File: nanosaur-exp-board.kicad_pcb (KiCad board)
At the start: 2 copper layers, 80 x 20 mm, 13 parts, among them J1 jetson_nano, J2 Screw_Terminal_01x02, J3 Conn_oled_right, J4 Conn_oled_left, J5 Conn_motors, J6 Conn_01x03, SW1 SW_SPDT

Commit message: minor fixes
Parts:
- J1: footprint Connector_PinSocket_2.54mm:PinSocket_2x21_P2.54mm_Vertical -> Connector_PinSocket_2.54mm:PinSocket_2x20_P2.54mm_Vertical
- moved J2 2.84 mm to (157.3, 92.8)
- moved J3 2.84 mm to (135.5, 86.0)
- moved J4 2.84 mm to (145.7, 86.0)
- moved J5 2.84 mm to (145.7, 89.8)
- moved J6 2.84 mm to (132.9, 89.8)
- moved R1 2.84 mm to (138.1, 92.8)
- moved R2 2.84 mm to (138.1, 95.1)
- moved J1 2.72 mm to (163.6, 97.9)
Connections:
- J1 pad 10: Net-(J1-Pad10) -> (no net)
- J1 pad 11: Net-(J1-Pad11) -> (no net)
- J1 pad 12: Net-(J1-Pad12) -> (no net)
- J1 pad 13: Net-(J1-Pad13) -> (no net)
- J1 pad 15: Net-(J1-Pad15) -> (no net)
- J1 pad 16: Net-(J1-Pad16) -> (no net)
- J1 pad 18: Net-(J1-Pad18) -> (no net)
- J1 pad 19: Net-(J1-Pad19) -> (no net)
- J1 pad 21: Net-(J1-Pad21) -> (no net)
- J1 pad 22: Net-(J1-Pad22) -> (no net)
- J1 pad 23: Net-(J1-Pad23) -> (no net)
- J1 pad 24: Net-(J1-Pad24) -> (no net)
- J1 pad 26: Net-(J1-Pad26) -> (no net)
- J1 pad 29: Net-(J1-Pad29) -> (no net)
- J1 pad 32: Net-(J1-Pad32) -> (no net)
- J1 pad 35: Net-(J1-Pad35) -> (no net)
- J1 pad 36: Net-(J1-Pad36) -> (no net)
- J1 pad 37: Net-(J1-Pad37) -> (no net)
- J1 pad 38: Net-(J1-Pad38) -> (no net)
- J1 pad 40: Net-(J1-Pad40) -> (no net)
- J1 pad 7: Net-(J1-Pad7) -> (no net)
- J1 pad 8: Net-(J1-Pad8) -> (no net)
- SW1 pad 3: Net-(SW1-Pad3) -> (no net)
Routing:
- net VCC: track 76.9 -> 64.9 mm
- net Net-(J2-Pad2): track 15.0 -> 16.7 mm

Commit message: Merge update from Mauro and minor fixes
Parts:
- J1: footprint Connector_PinSocket_2.54mm:PinSocket_2x20_P2.54mm_Vertical -> Connector_PinSocket_2.54mm:PinSocket_2x21_P2.54mm_Vertical
- moved J2 2.84 mm to (160.0, 91.9)
- moved J4 2.84 mm to (148.4, 85.2)
- moved J5 2.84 mm to (148.4, 89.0)
- moved J6 2.84 mm to (135.6, 88.9)
- moved R1 2.84 mm to (140.8, 91.9)
- moved R2 2.84 mm to (140.8, 94.2)
- moved J1 2.72 mm to (166.2, 97.0)
- moved J3 1.87 mm to (137.2, 85.2)
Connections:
- J1 pad 10: (no net) -> Net-(J1-Pad10)
- J1 pad 11: (no net) -> Net-(J1-Pad11)
- J1 pad 12: (no net) -> Net-(J1-Pad12)
- J1 pad 13: (no net) -> Net-(J1-Pad13)
- J1 pad 15: (no net) -> Net-(J1-Pad15)
- J1 pad 16: (no net) -> Net-(J1-Pad16)
- J1 pad 18: (no net) -> Net-(J1-Pad18)
- J1 pad 19: (no net) -> Net-(J1-Pad19)
- J1 pad 21: (no net) -> Net-(J1-Pad21)
- J1 pad 22: (no net) -> Net-(J1-Pad22)
- J1 pad 23: (no net) -> Net-(J1-Pad23)
- J1 pad 24: (no net) -> Net-(J1-Pad24)
- J1 pad 26: (no net) -> Net-(J1-Pad26)
- J1 pad 29: (no net) -> Net-(J1-Pad29)
- J1 pad 32: (no net) -> Net-(J1-Pad32)
- J1 pad 35: (no net) -> Net-(J1-Pad35)
- J1 pad 36: (no net) -> Net-(J1-Pad36)
- J1 pad 37: (no net) -> Net-(J1-Pad37)
- J1 pad 38: (no net) -> Net-(J1-Pad38)
- J1 pad 40: (no net) -> Net-(J1-Pad40)
- J1 pad 7: (no net) -> Net-(J1-Pad7)
- J1 pad 8: (no net) -> Net-(J1-Pad8)
- SW1 pad 3: (no net) -> Net-(SW1-Pad3)
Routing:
- net GND: track 3.81 -> 131.6 mm, vias 0 -> 1
- net +3V3: track 9.93 -> 37.8 mm, vias 0 -> 2
- net VCC: track 64.9 -> 77.6 mm
- net Net-(J2-Pad2): track 16.7 -> 15.0 mm
- net Net-(J1-Pad28): track 18.8 -> 19.4 mm, vias 0 -> 1
- added copper zone on B.Cu, net GND
- added copper zone on F.Cu, net GND
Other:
- net class POWER added: clearance 0.2, trace_width 0.35, via_dia 0.8, via_drill 0.4

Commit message: Improve sch and pcb
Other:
- board text added: "Nanosaur expansion board"
- board text added: "Raffaello Bonghi"
- board text added: "v1.0"

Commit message: Improve pcb
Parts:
- moved SW1 0.88 mm to (171.6, 94.2)
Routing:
- net VCC: track 77.6 -> 76.2 mm

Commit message: Improve sch and pcb
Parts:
- added G***: LOGO, nanosaur:nanosaur_logo, F.Cu at (121.2, 91.8)
- added H5: MountingHole, MountingHole:MountingHole_2.2mm_M2, F.Cu at (116.0, 85.8)
- added H6: MountingHole, MountingHole:MountingHole_2.2mm_M2, F.Cu at (122.0, 85.8)
- added J7: Conn_01x04, Connector_PinHeader_2.54mm:PinHeader_1x04_P2.54mm_Vertical, F.Cu at (147.5, 93.2)
- H1, H2, H3, H4: footprint MountingHole:MountingHole_2.2mm_M2_ISO7380_Pad -> MountingHole:MountingHole_2.2mm_M2
- J3: value Conn_oled_right -> Conn_01x04
- J4: value Conn_oled_left -> Conn_01x04
- J5: value Conn_motors -> Conn_01x06; footprint Connector_PinHeader_2.54mm:PinHeader_1x04_P2.54mm_Vertical -> Connector_PinHeader_2.54mm:PinHeader_1x06_P2.54mm_Vertical
- moved J5 4.25 mm to (152.6, 89.5)
- moved R2 3.81 mm to (137.1, 94.6)
- moved R1 3.80 mm to (137.1, 92.4)
- moved J2 2.59 mm to (160.1, 94.5)
- moved J6 2.08 mm to (133.6, 89.5)
- moved J1 1.41 mm to (166.6, 98.4)
- moved J3 1.16 mm to (136.2, 85.8)
- moved J4 1.10 mm to (147.5, 85.8)
- moved SW1 0.20 mm to (171.6, 94.4)
- moved H1 0.06 mm to (109.0, 85.3)
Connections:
- J1 pad 10: Net-(J1-Pad10) -> (no net)
- J1 pad 11: Net-(J1-Pad11) -> (no net)
- J1 pad 12: Net-(J1-Pad12) -> (no net)
- J1 pad 13: Net-(J1-Pad13) -> (no net)
- J1 pad 15: Net-(J1-Pad15) -> (no net)
- J1 pad 16: Net-(J1-Pad16) -> (no net)
- J1 pad 18: Net-(J1-Pad18) -> (no net)
- J1 pad 19: Net-(J1-Pad19) -> (no net)
- J1 pad 21: Net-(J1-Pad21) -> (no net)
- J1 pad 22: Net-(J1-Pad22) -> (no net)
- J1 pad 23: Net-(J1-Pad23) -> (no net)
- J1 pad 24: Net-(J1-Pad24) -> (no net)
- J1 pad 26: Net-(J1-Pad26) -> (no net)
- J1 pad 29: Net-(J1-Pad29) -> (no net)
- J1 pad 32: Net-(J1-Pad32) -> (no net)
- J1 pad 35: Net-(J1-Pad35) -> (no net)
- J1 pad 36: Net-(J1-Pad36) -> (no net)
- J1 pad 37: Net-(J1-Pad37) -> (no net)
- J1 pad 38: Net-(J1-Pad38) -> (no net)
- J1 pad 40: Net-(J1-Pad40) -> (no net)
- J1 pad 7: Net-(J1-Pad7) -> (no net)
- J1 pad 8: Net-(J1-Pad8) -> (no net)
- J3 pad 3: VCC -> +3V3
- J4 pad 3: VCC -> +3V3
- J5 pad 1: Net-(J1-Pad3) -> VCC
- J5 pad 2: Net-(J1-Pad5) -> GND
- J5 pad 3: VCC -> Net-(J1-Pad3)
- J5 pad 4: GND -> Net-(J1-Pad5)
- SW1 pad 3: Net-(SW1-Pad3) -> (no net)
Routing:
- net GND: track 131.6 -> 88.2 mm, vias 1 -> 0
- net VCC: track 76.2 -> 48.3 mm
- net +3V3: track 37.8 -> 63.1 mm, vias 2 -> 0
- net Net-(J2-Pad2): track 15.0 -> 17.7 mm
- net Net-(J1-Pad31): track 15.0 -> 12.3 mm
- net Net-(J1-Pad33): track 15.3 -> 12.7 mm
- net Net-(J1-Pad27): track 16.5 -> 14.5 mm
- net Net-(J1-Pad5): track 25.5 -> 27.2 mm
- net Net-(J1-Pad3): track 26.2 -> 27.7 mm
- net Net-(J1-Pad28): track 19.4 -> 19.6 mm, vias 1 -> 0
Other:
- outline, holes or cut-outs redrawn
- net class 3.3 line added: clearance 0.2, trace_width 0.45, via_dia 0.8, via_drill 0.4
- net class POWER: trace_width 0.35 -> 1.3

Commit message: Improve sch and azz gerber zip
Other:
- board text added: "(C)2021 Raffaello Bonghi"
- board text added: "nanosaur.ai"
- board text removed: "Raffaello Bonghi"

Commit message: Fix kibot and pcb
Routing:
- net GND: track 88.2 -> 84.2 mm
- net Net-(J2-Pad2): track 17.7 -> 14.8 mm
- net VCC: track 48.3 -> 46.2 mm

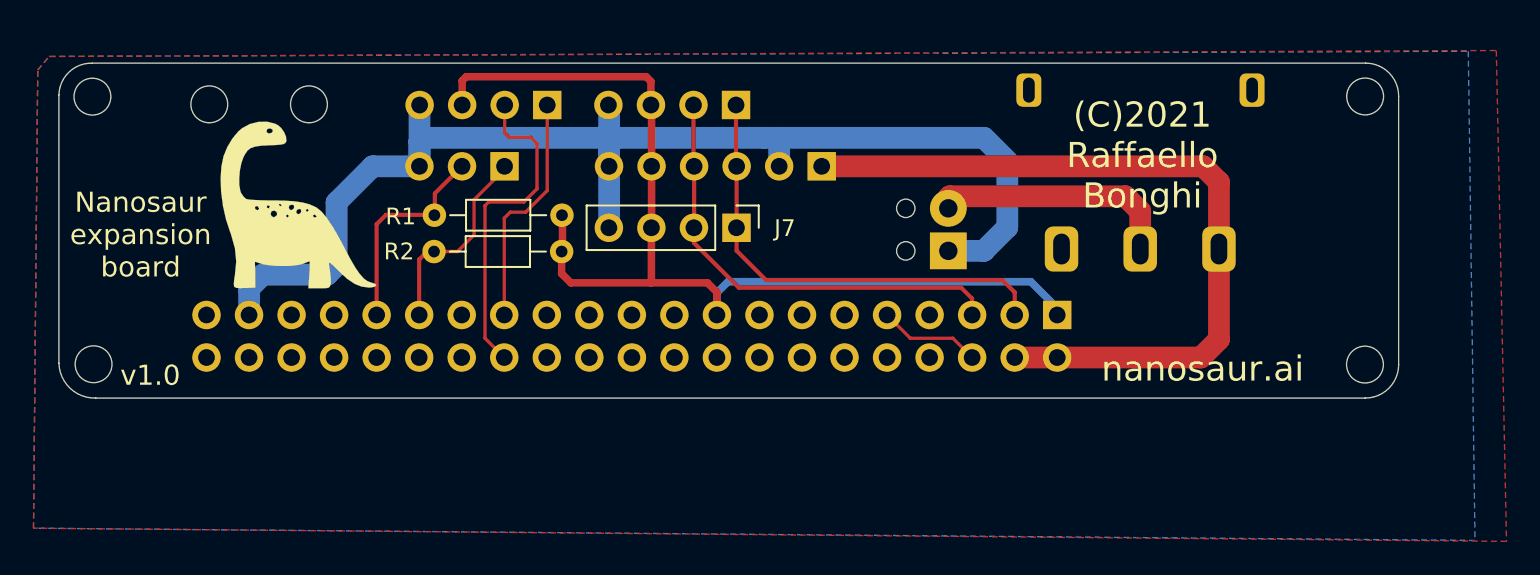
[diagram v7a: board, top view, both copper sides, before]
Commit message: Improve PCB layout, fix BOM, improve sch
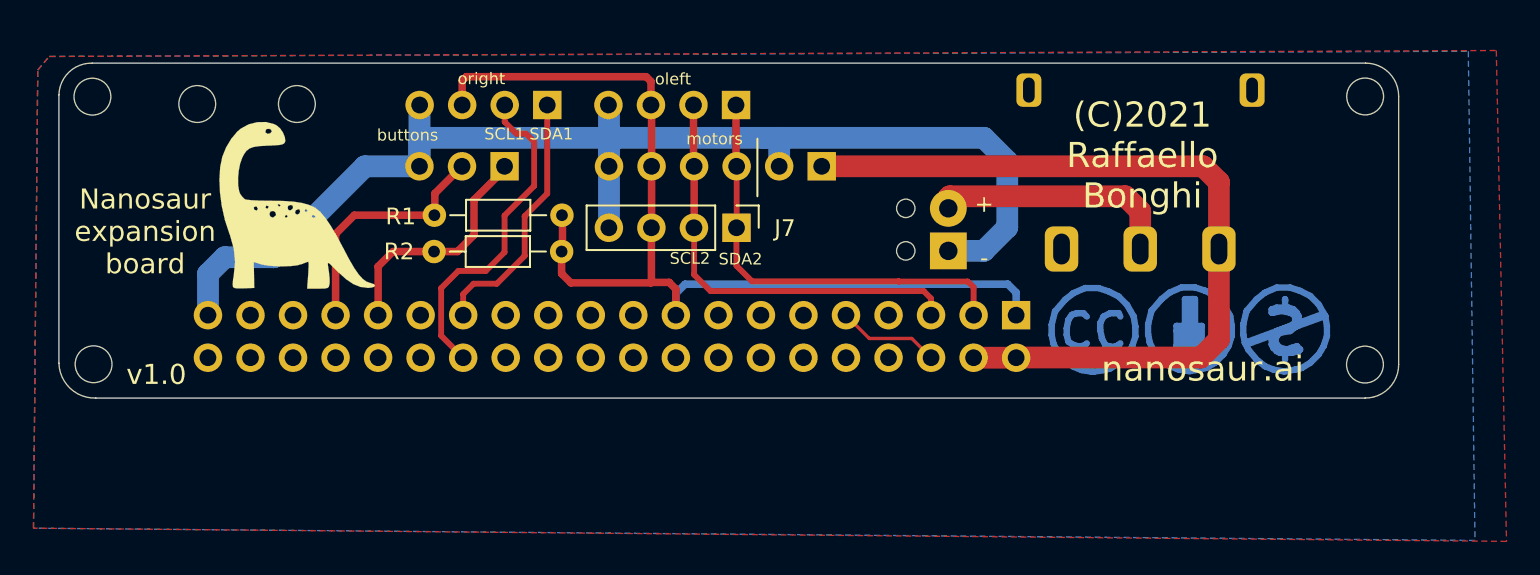
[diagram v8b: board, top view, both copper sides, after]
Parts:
- added G***: LOGO, nanosaur:officinerobotiche, B.Cu at (111.3, 91.8)
- added REF**: Symbol_CreativeCommons_CopperTop_Type2_Small, Symbol:Symbol_CreativeCommons_CopperTop_Type2_Small, B.Cu at (168.7, 99.2)
- added REF**: Symbol_CC-Noncommercial_CopperTop_Small, Symbol:Symbol_CC-Noncommercial_CopperTop_Small, B.Cu at (180.2, 99.2)
- added REF**: Symbol_CC-Attribution_CopperTop_Small, Symbol:Symbol_CC-Attribution_CopperTop_Small, B.Cu at (174.6, 99.2)
- J1: footprint Connector_PinSocket_2.54mm:PinSocket_2x21_P2.54mm_Vertical -> Connector_PinSocket_2.54mm:PinSocket_2x20_P2.54mm_Vertical
- J3, J4: value Conn_01x04 -> Conn_i2c_oled
- J5: value Conn_01x06 -> Conn_motors
- J6: value Conn_01x03 -> Conn_buttons
- moved J1 2.45 mm to (164.2, 98.4)
- moved H5 0.72 mm to (115.3, 85.8)
- moved H6 0.72 mm to (121.2, 85.8)
- moved G*** 0.07 mm to (121.1, 91.8)
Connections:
- J1 pad 10: (no net) -> Net-(J1-Pad10)
- J1 pad 11: (no net) -> Net-(J1-Pad11)
- J1 pad 12: (no net) -> Net-(J1-Pad12)
- J1 pad 13: (no net) -> Net-(J1-Pad13)
- J1 pad 15: (no net) -> Net-(J1-Pad15)
- J1 pad 16: (no net) -> Net-(J1-Pad16)
- J1 pad 18: (no net) -> Net-(J1-Pad18)
- J1 pad 19: (no net) -> Net-(J1-Pad19)
- J1 pad 21: (no net) -> Net-(J1-Pad21)
- J1 pad 22: (no net) -> Net-(J1-Pad22)
- J1 pad 23: (no net) -> Net-(J1-Pad23)
- J1 pad 24: (no net) -> Net-(J1-Pad24)
- J1 pad 26: (no net) -> Net-(J1-Pad26)
- J1 pad 29: (no net) -> Net-(J1-Pad29)
- J1 pad 32: (no net) -> Net-(J1-Pad32)
- J1 pad 35: (no net) -> Net-(J1-Pad35)
- J1 pad 36: (no net) -> Net-(J1-Pad36)
- J1 pad 37: (no net) -> Net-(J1-Pad37)
- J1 pad 38: (no net) -> Net-(J1-Pad38)
- J1 pad 40: (no net) -> Net-(J1-Pad40)
- J1 pad 7: (no net) -> Net-(J1-Pad7)
- J1 pad 8: (no net) -> Net-(J1-Pad8)
- SW1 pad 3: (no net) -> Net-(SW1-Pad3)
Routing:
- net Net-(J1-Pad31): track 12.3 -> 15.1 mm
- net +3V3: track 63.1 -> 60.6 mm
- net VCC: track 46.2 -> 48.6 mm
- net Net-(J1-Pad33): track 12.7 -> 14.8 mm
- net Net-(J1-Pad3): track 27.7 -> 26.0 mm
- net Net-(J1-Pad5): track 27.2 -> 25.9 mm
- net Net-(J1-Pad27): track 14.5 -> 15.8 mm
- net GND: track 84.2 -> 85.0 mm
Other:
- board text added: "+"
- board text added: "+ -"
- board text added: "SCL1"
- board text added: "SCL2"
- board text added: "SDA1"
- board text added: "SDA2"
- board text added: "buttons"
- board text added: "motors"
- board text added: "oleft"
- board text added: "oright"
